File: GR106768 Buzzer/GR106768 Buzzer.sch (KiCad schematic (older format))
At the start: 172 parts, among them IC1 LMC7211, IC2 MC33172, IC3 MC33172, IC4 LMV321, J1 to CPU board, J2 MIRECMS, J3 MIRECMS, T1 BC847, T2 BC857, T3 BC847, T4 BC857

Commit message: rename pad hole according to conventions
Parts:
- H1, H10, H100, H101, H102, H103, H104, H105, H11, H12, H13, H14, H15, H16, H17, H18, H19, H2, H20, H21, H22, H23, H24, H25, H26, H27, H28, H29, H3, H30, H31, H32, H33, H34, H35, H36, H37, H38, H39, H4, H40, H41, H42, H43, H44, H45, H46, H47, H48, H49, H5, H50, H51, H52, H53, H54, H55, H56, H57, H58, H59, H6, H60, H61, H62, H63, H64, H65, H66, H67, H68, H69, H7, H70, H71, H72, H73, H74, H75, H76, H77, H78, H79, H8, H80, H81, H82, H83, H84, H85, H86, H87, H88, H89, H9, H90, H91, H92, H93, H94, H95, H96, H97, H98, H99: footprint GR106768 Buzzer:PadHole -> GR106768 Buzzer:ThroughHole_60milx12mil_Pad_Cu_Mask

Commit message: rename c0402 as it differs from global fp library
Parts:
- C10, C11, C2, C30, C4, C5, C6, C7, C8, C9: footprint GR106768 Buzzer:C0402_1 -> GR106768 Buzzer:C0402_1b
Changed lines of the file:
@@
 F 0 "C4" H 6000 3375 50  0000 L CNN
 F 1 "680pF" H 5975 3175 50  0000 L CNN
-F 2 "GR106768 Buzzer:C0402_1" H 5988 3125 50  0001 C CNN
+F 2 "GR106768 Buzzer:C0402_1b" H 5988 3125 50  0001 C CNN
 F 3 "~" H 5950 3275 50  0001 C CNN
     1    5950 3275
@@
 F 0 "C10" V 2025 5300 50  0000 L CNN
 F 1 "100nF" V 1725 5200 50  0000 L CNN
-F 2 "GR106768 Buzzer:C0402_1" H 1913 5200 50  0001 C CNN
+F 2 "GR106768 Buzzer:C0402_1b" H 1913 5200 50  0001 C CNN
 F 3 "~" H 1875 5350 50  0001 C CNN
     1    1875 5350
@@
 F 0 "C5" V 6050 4325 50  0000 L CNN
 F 1 "100nF" V 6275 4150 50  0000 L CNN
-F 2 "GR106768 Buzzer:C0402_1" H 6163 4100 50  0001 C CNN
+F 2 "GR106768 Buzzer:C0402_1b" H 6163 4100 50  0001 C CNN
 F 3 "~" H 6125 4250 50  0001 C CNN
     1    6125 4250
@@
 F 0 "C9" V 7775 4375 50  0000 L CNN
 F 1 "100nF" V 7475 4325 50  0000 L CNN
-F 2 "GR106768 Buzzer:C0402_1" H 7663 4300 50  0001 C CNN
+F 2 "GR106768 Buzzer:C0402_1b" H 7663 4300 50  0001 C CNN
 F 3 "~" H 7625 4450 50  0001 C CNN
     1    7625 4450
@@
 F 0 "C30" V 14475 6425 50  0000 L CNN
 F 1 "100nF" V 14150 6475 50  0000 L CNN
-F 2 "GR106768 Buzzer:C0402_1" H 14363 6425 50  0001 C CNN
+F 2 "GR106768 Buzzer:C0402_1b" H 14363 6425 50  0001 C CNN
 F 3 "~" H 14325 6575 50  0001 C CNN
     1    14325 6575
@@
 F 0 "C6" V 6750 2325 50  0000 L CNN
 F 1 "680pF" V 6425 2275 50  0000 L CNN
-F 2 "GR106768 Buzzer:C0402_1" H 6638 2250 50  0001 C CNN
+F 2 "GR106768 Buzzer:C0402_1b" H 6638 2250 50  0001 C CNN
 F 3 "~" H 6600 2400 50  0001 C CNN
     1    6600 2400
@@
 F 0 "C11" V 2025 6200 50  0000 L CNN
 F 1 "100nF" V 1725 6125 50  0000 L CNN
-F 2 "GR106768 Buzzer:C0402_1" H 1913 6100 50  0001 C CNN
+F 2 "GR106768 Buzzer:C0402_1b" H 1913 6100 50  0001 C CNN
 F 3 "~" H 1875 6250 50  0001 C CNN
     1    1875 6250
@@
 F 0 "C7" V 3600 5300 50  0000 L CNN
 F 1 "100nF" V 3300 5200 50  0000 L CNN
-F 2 "GR106768 Buzzer:C0402_1" H 3488 5200 50  0001 C CNN
+F 2 "GR106768 Buzzer:C0402_1b" H 3488 5200 50  0001 C CNN
 F 3 "~" H 3450 5350 50  0001 C CNN
     1    3450 5350
@@
 F 0 "C8" V 3600 6200 50  0000 L CNN
 F 1 "100nF" V 3300 6125 50  0000 L CNN
-F 2 "GR106768 Buzzer:C0402_1" H 3488 6100 50  0001 C CNN
+F 2 "GR106768 Buzzer:C0402_1b" H 3488 6100 50  0001 C CNN
 F 3 "~" H 3450 6250 50  0001 C CNN
     1    3450 6250
@@
 F 0 "C2" H 4365 3571 50  0000 L CNN
 F 1 "220pF" H 4300 3425 50  0000 L CNN
-F 2 "GR106768 Buzzer:C0402_1" H 4288 3375 50  0001 C CNN
+F 2 "GR106768 Buzzer:C0402_1b" H 4288 3375 50  0001 C CNN
 F 3 "~" H 4250 3525 50  0001 C CNN
     1    4250 3525

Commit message: rename c0603 as it differs from global fp library
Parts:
- C13, C14: footprint GR106768 Buzzer:C0603_1 -> GR106768 Buzzer:C0603_1b
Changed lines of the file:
@@
 F 0 "C13" H 11625 6950 50  0000 L CNN
 F 1 "33nF" H 11575 7175 50  0000 L CNN
-F 2 "GR106768 Buzzer:C0603_1" H 11838 6900 50  0001 C CNN
+F 2 "GR106768 Buzzer:C0603_1b" H 11838 6900 50  0001 C CNN
 F 3 "~" H 11800 7050 50  0001 C CNN
     1    11800 7050
@@
 F 0 "C14" V 12100 5425 50  0000 L CNN
 F 1 "33nF" V 12400 5425 50  0000 L CNN
-F 2 "GR106768 Buzzer:C0603_1" H 12288 5350 50  0001 C CNN
+F 2 "GR106768 Buzzer:C0603_1b" H 12288 5350 50  0001 C CNN
 F 3 "~" H 12250 5500 50  0001 C CNN
     1    12250 5500

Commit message: rename rc0805 as it differs from global fp library
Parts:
- C3: footprint GR106768 Buzzer:C0805_1 -> GR106768 Buzzer:C0805_1b
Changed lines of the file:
@@
 F 0 "C3" H 5400 6000 50  0000 L CNN
 F 1 "10nF" H 5400 5800 50  0000 L CNN
-F 2 "GR106768 Buzzer:C0805_1" H 5388 5750 50  0001 C CNN
+F 2 "GR106768 Buzzer:C0805_1b" H 5388 5750 50  0001 C CNN
 F 3 "~" H 5350 5900 50  0001 C CNN
     1    5350 5900

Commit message: update fp libpaths
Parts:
- BUZ1, BUZ2: footprint GR106768 Buzzer:PKM33EPH-1201C_1 -> AllModules:PKM33EPH-1201C_1
- C1: footprint GR106768 Buzzer:C0612-4_1 -> AllModules:C0612-4_1
- C10, C11, C2, C30, C4, C5, C6, C7, C8, C9: footprint GR106768 Buzzer:C0402_1b -> AllModules:C0402_1b
- C12: footprint GR106768 Buzzer:AX10X30_1 -> AllModules:AX10X30_1
- C13, C14: footprint GR106768 Buzzer:C0603_1b -> AllModules:C0603_1b
- C3: footprint GR106768 Buzzer:C0805_1b -> AllModules:C0805_1b
- D1: footprint GR106768 Buzzer:DO216AA_1 -> AllModules:DO216AA_1
- D2, D3, D4, D5: footprint GR106768 Buzzer:SOT23-1G_1 -> AllModules:SOT23-1G_1
- FI1: footprint GR106768 Buzzer:WE-FA_1 -> AllModules:WE-FA_1
- FU1: footprint GR106768 Buzzer:F6126_1 -> AllModules:F6126_1
- H1, H10, H100, H101, H102, H103, H104, H105, H11, H12, H13, H14, H15, H16, H17, H18, H19, H2, H20, H21, H22, H23, H24, H25, H26, H27, H28, H29, H3, H30, H31, H32, H33, H34, H35, H36, H37, H38, H39, H4, H40, H41, H42, H43, H44, H45, H46, H47, H48, H49, H5, H50, H51, H52, H53, H54, H55, H56, H57, H58, H59, H6, H60, H61, H62, H63, H64, H65, H66, H67, H68, H69, H7, H70, H71, H72, H73, H74, H75, H76, H77, H78, H79, H8, H80, H81, H82, H83, H84, H85, H86, H87, H88, H89, H9, H90, H91, H92, H93, H94, H95, H96, H97, H98, H99: footprint GR106768 Buzzer:ThroughHole_60milx12mil_Pad_Cu_Mask -> AllModules:ThroughHole_60milx12mil_Pad_Cu_Mask
- IC1, IC4: footprint GR106768 Buzzer:SOT23-5_1 -> AllModules:SOT23-5_1
- IC2, IC3: footprint GR106768 Buzzer:MX.A8_COMPOSANT_1 -> AllModules:MX.A8_COMPOSANT_1
- J1: footprint GR106768 Buzzer:BAR7-3-2-COVIDIEN_1 -> AllModules:BAR7-3-2-COVIDIEN_1
- J2, J3: footprint GR106768 Buzzer:MIRECMS-SAFT_1 -> AllModules:MIRECMS-SAFT_1
- L1: footprint GR106768 Buzzer:RC1206_1 -> AllModules:RC1206_1
- R1, R10, R11, R12, R13, R14, R15, R16, R17, R18, R19, R2, R20, R21, R22, R23, R24, R25, R26, R27, R28, R29, R3, R4, R5, R59, R6, R69, R7, R8, R9: footprint GR106768 Buzzer:R0402_1 -> AllModules:R0402_1
- T1, T2, T3, T4: footprint GR106768 Buzzer:SOT23-BEC_1 -> AllModules:SOT23-BEC_1

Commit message: fix erc buzzer
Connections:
- wire segments 253 -> 256

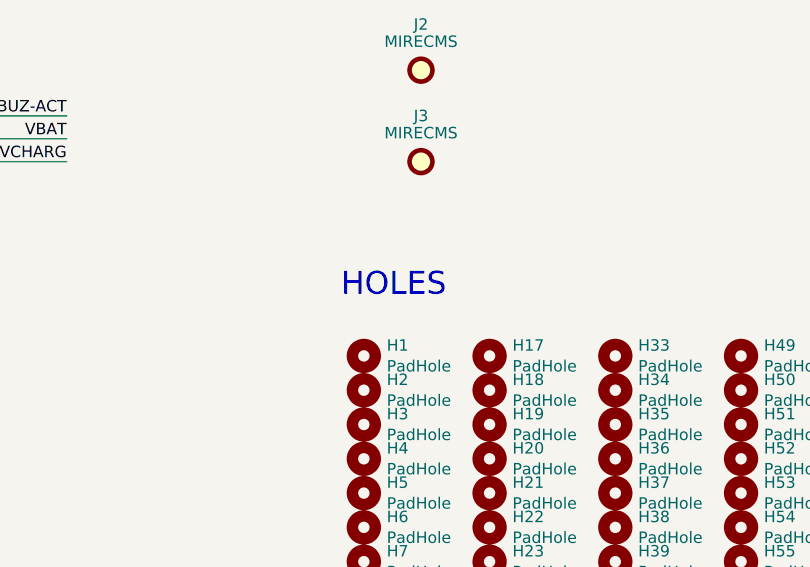
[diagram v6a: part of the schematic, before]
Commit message: fix erc errors, change many pin electrical types
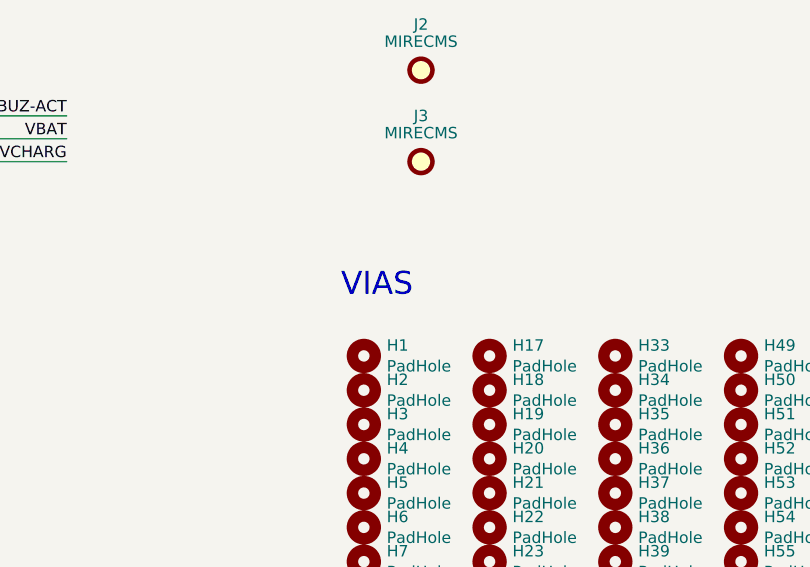
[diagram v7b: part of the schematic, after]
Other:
- note added: "VIAS"
- note removed: "HOLES"
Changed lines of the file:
@@
 FIDUCIALS
 Text Notes 6800 8500 0    100  ~ 0
-HOLES
+VIAS
 $Comp
 L Mechanical:MountingHole H1

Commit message: Buzzer dev
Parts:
- removed C1: 47pF, AllModules:C0612-4_1, symbol GR106768_Buzzer:C_NETWORK
- removed D1: NC, AllModules:DO216AA_1, symbol Device:D_Zener
- removed D2: BAT54C, AllModules:SOT23-1G_1, symbol Diode:BAT54C
- removed D3, D4: BAT54S, AllModules:SOT23-1G_1, symbol Diode:BAT54S
- removed D5: BZX84C2V7, AllModules:SOT23-1G_1, symbol Device:D_Zener
- removed FI1: BLA31BD221SN4D, AllModules:WE-FA_1, symbol GR106768_Buzzer:BLA31BD221SN4D
- removed T1, T3: BC847, AllModules:SOT23-BEC_1, symbol Transistor_BJT:BC847
- removed T2, T4: BC857, AllModules:SOT23-BEC_1, symbol Transistor_BJT:BC857
- added C1: 47pF, AllModules:C0612-4_1, symbol GR106768_Buzzer:C-array4-0612_47p
- added D1: NC, AllModules:DO216AA_1, symbol GR106768_Buzzer:MBRM120
- added D2: BAT54C, AllModules:SOT23-1G_1, symbol GR106768_Buzzer:BAT54C
- added D3, D4: BAT54S, AllModules:SOT23-1G_1, symbol GR106768_Buzzer:BAT54S
- added D5: BZX84C2V7, AllModules:SOT23-1G_1, symbol GR106768_Buzzer:BZX84C2V7
- added FI1: BK32164M102-T, AllModules:WE-FA_1, symbol GR106768_Buzzer:BK3216xxxxx
- added T1, T3: BC847, AllModules:SOT23-BEC_1, symbol GR106768_Buzzer:BC847
- added T2, T4: BC857, AllModules:SOT23-BEC_1, symbol GR106768_Buzzer:BC857
- BUZ1, BUZ2: Item Number (none) -> 10022130; MPN muRATA PKM33EPH-1201C -> (none)
- C12: symbol Device:CP -> GR106768_Buzzer:Celec-axial-10x30_470u
- IC1: Item Number (none) -> 10099025
- R69: footprint AllModules:R0402_1 -> GR106768 Buzzer:R0402_1
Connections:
- net labels added: +5V_CPU, INHIB-STOP-INV-CPU, PWM-BUZ, PWM-BUZZER-CPU, STOP-INV-CPU, SUPPLY-BUZ-CPU, TEST-BUZZER-CPU
- wire segments 256 -> 261
- no-connect marks 0 -> 2
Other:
- note added: "Should FI1 have the BLA2AAG102 part\nnumber? I thought the Master BOM\nsaid it was obsolete, but maybe there\nis stock available?"
- moved on the sheet: C3, C4, C5, C9, FU1, IC3A, L1, R10, R11, R12, R13, R14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
